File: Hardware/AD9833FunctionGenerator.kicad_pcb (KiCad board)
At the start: 2 copper layers, 125.7 x 114.3 mm, 53 parts, among them U1 LM7805_TO220

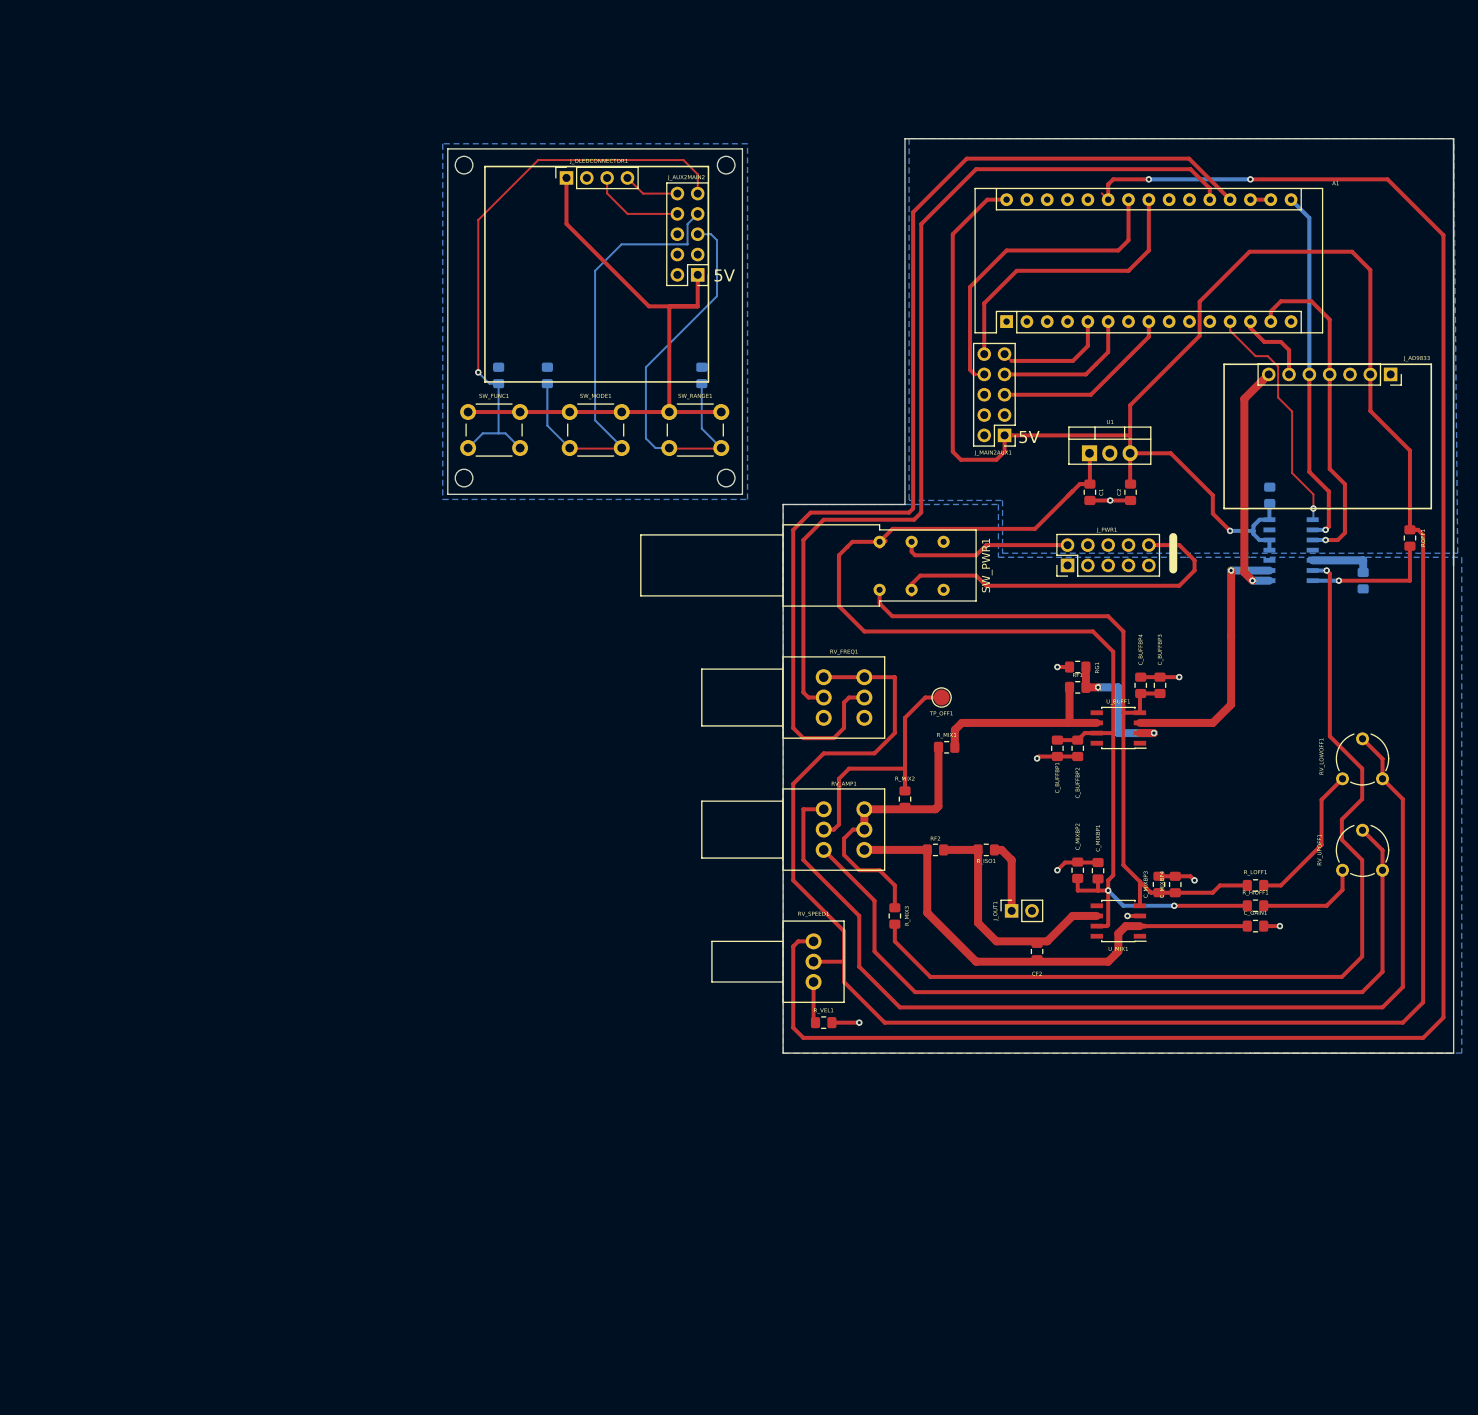
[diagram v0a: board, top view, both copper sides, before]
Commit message: Updated potentimeter footprints
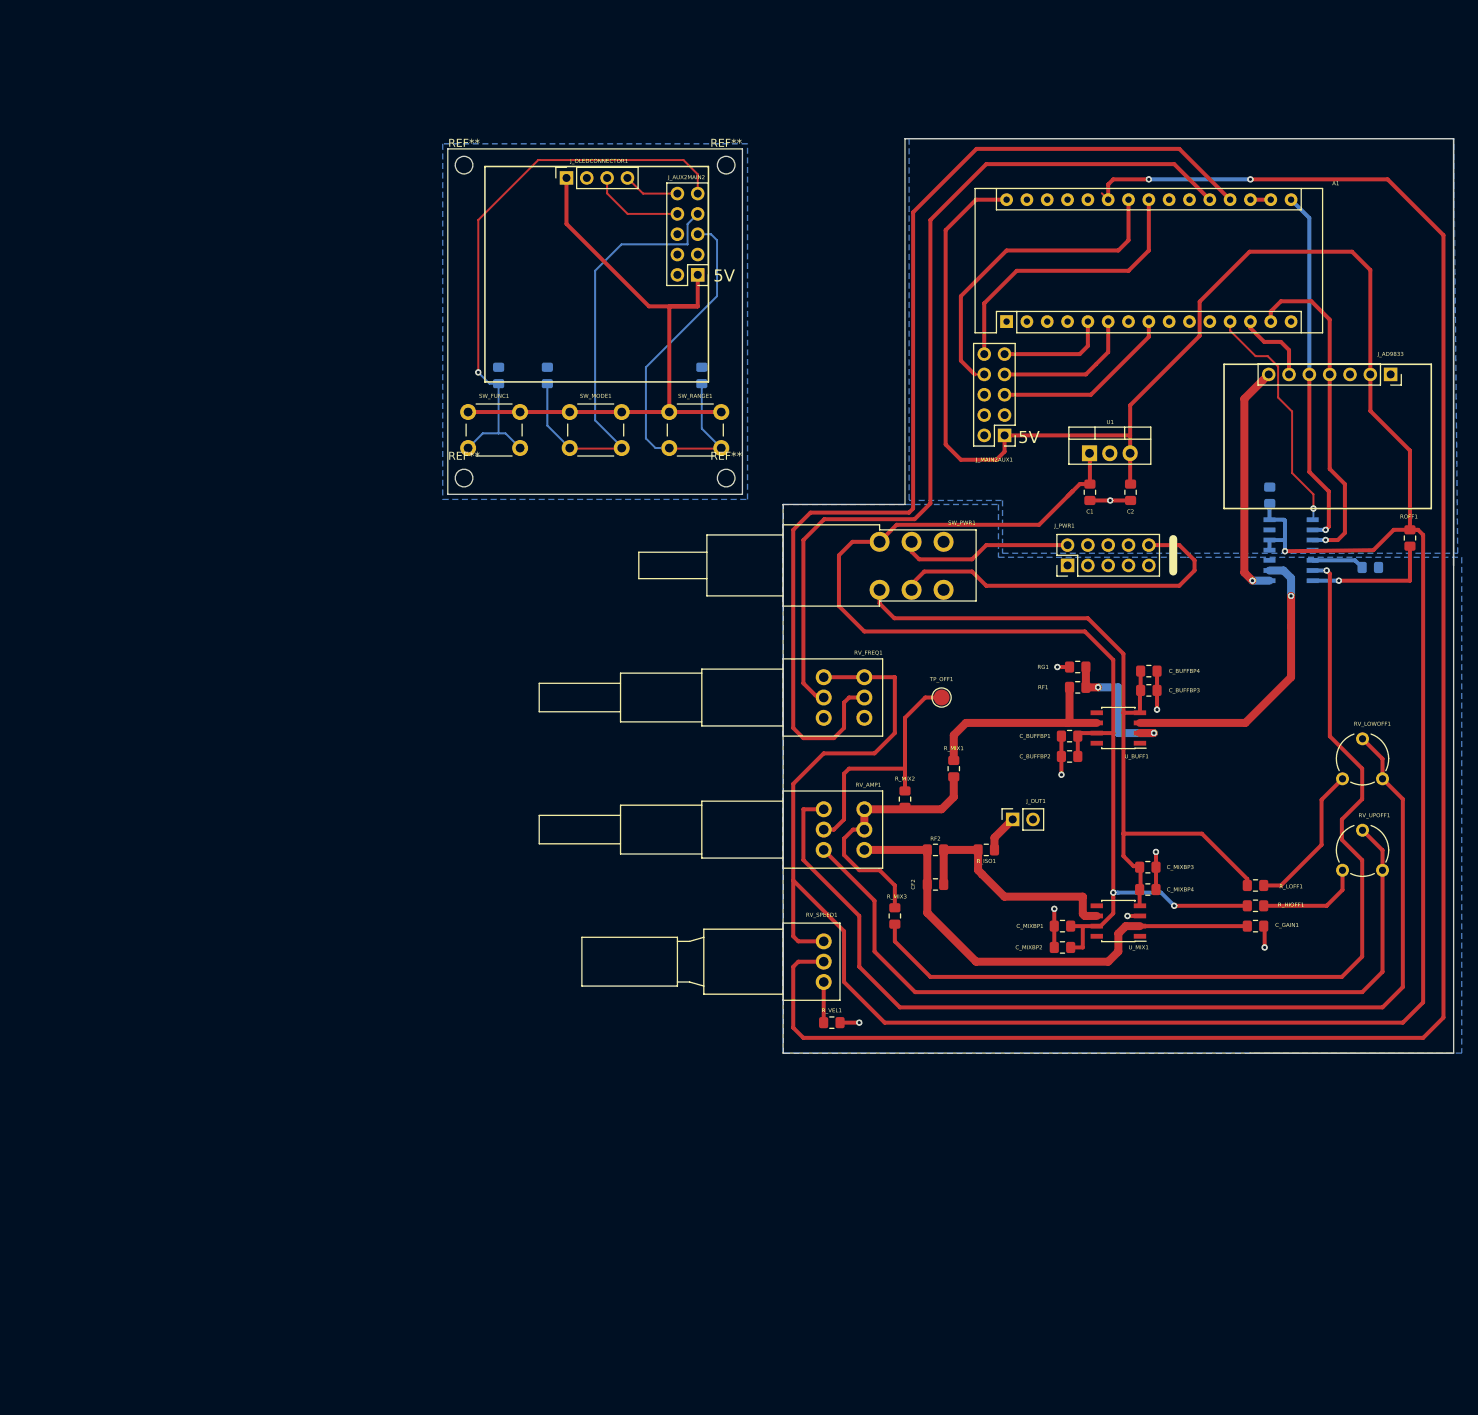
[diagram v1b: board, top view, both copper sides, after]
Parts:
- moved CF2 15.2 mm to (138.4, 128.8), turned to 180 degrees
- moved J_OUT1 11.4 mm to (148.1, 120.7)
- moved C_MIXBP2 9.84 mm to (154.3, 136.7), turned to 180 degrees
- moved C_MIXBP1 8.23 mm to (154.3, 134.0), turned to 180 degrees
- moved C_MIXBP4 3.49 mm to (165.0, 129.4), turned to 0 degrees
- moved R_MIX1 2.81 mm to (140.7, 114.3), turned to 270 degrees
- moved C_MIXBP3 2.57 mm to (165.0, 126.6), turned to 0 degrees
- moved C_BUFFBP1 2.16 mm to (155.2, 110.2), turned to 180 degrees
- moved C_BUFFBP4 2.05 mm to (165.1, 102.1), turned to 0 degrees
- moved ROFF2 1.88 mm to (192.8, 89.2), turned to 0 degrees
- moved C_BUFFBP3 1.53 mm to (165.1, 104.5), turned to 0 degrees
- moved C_BUFFBP2 1.44 mm to (155.2, 112.8), turned to 180 degrees
- moved R_VEL1 1.02 mm to (125.5, 146.1)
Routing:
- net /5V: track 375.8 -> 382.6 mm
- net /OutputSection/SIGOUT: track 9.03 -> 4.75 mm
- net /-12V: track 89.5 -> 92.5 mm
- net /DDS_REDUX: track 34.5 -> 37.2 mm
- net Net-(RV_AMP1-Pad5): track 35.1 -> 32.6 mm
- net /+12V: track 152.1 -> 150.6 mm
- net /FREQ2: track 115.4 -> 114.0 mm
- net Net-(ROFF2-Pad1): track 7.83 -> 6.55 mm
- net /VEL1: track 241.7 -> 240.4 mm
- net /AGND: track 28.5 -> 27.3 mm
- net /WAVEBTN: track 14.6 -> 13.4 mm
- net /FREQ1: track 135.8 -> 136.8 mm
- net /SCL: track 39.7 -> 40.6 mm
- net Net-(CF2-Pad1): track 30.5 -> 29.6 mm
- net Net-(RF1-Pad1): track 25.6 -> 26.2 mm

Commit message: Added third concentric dual pot for phase feature
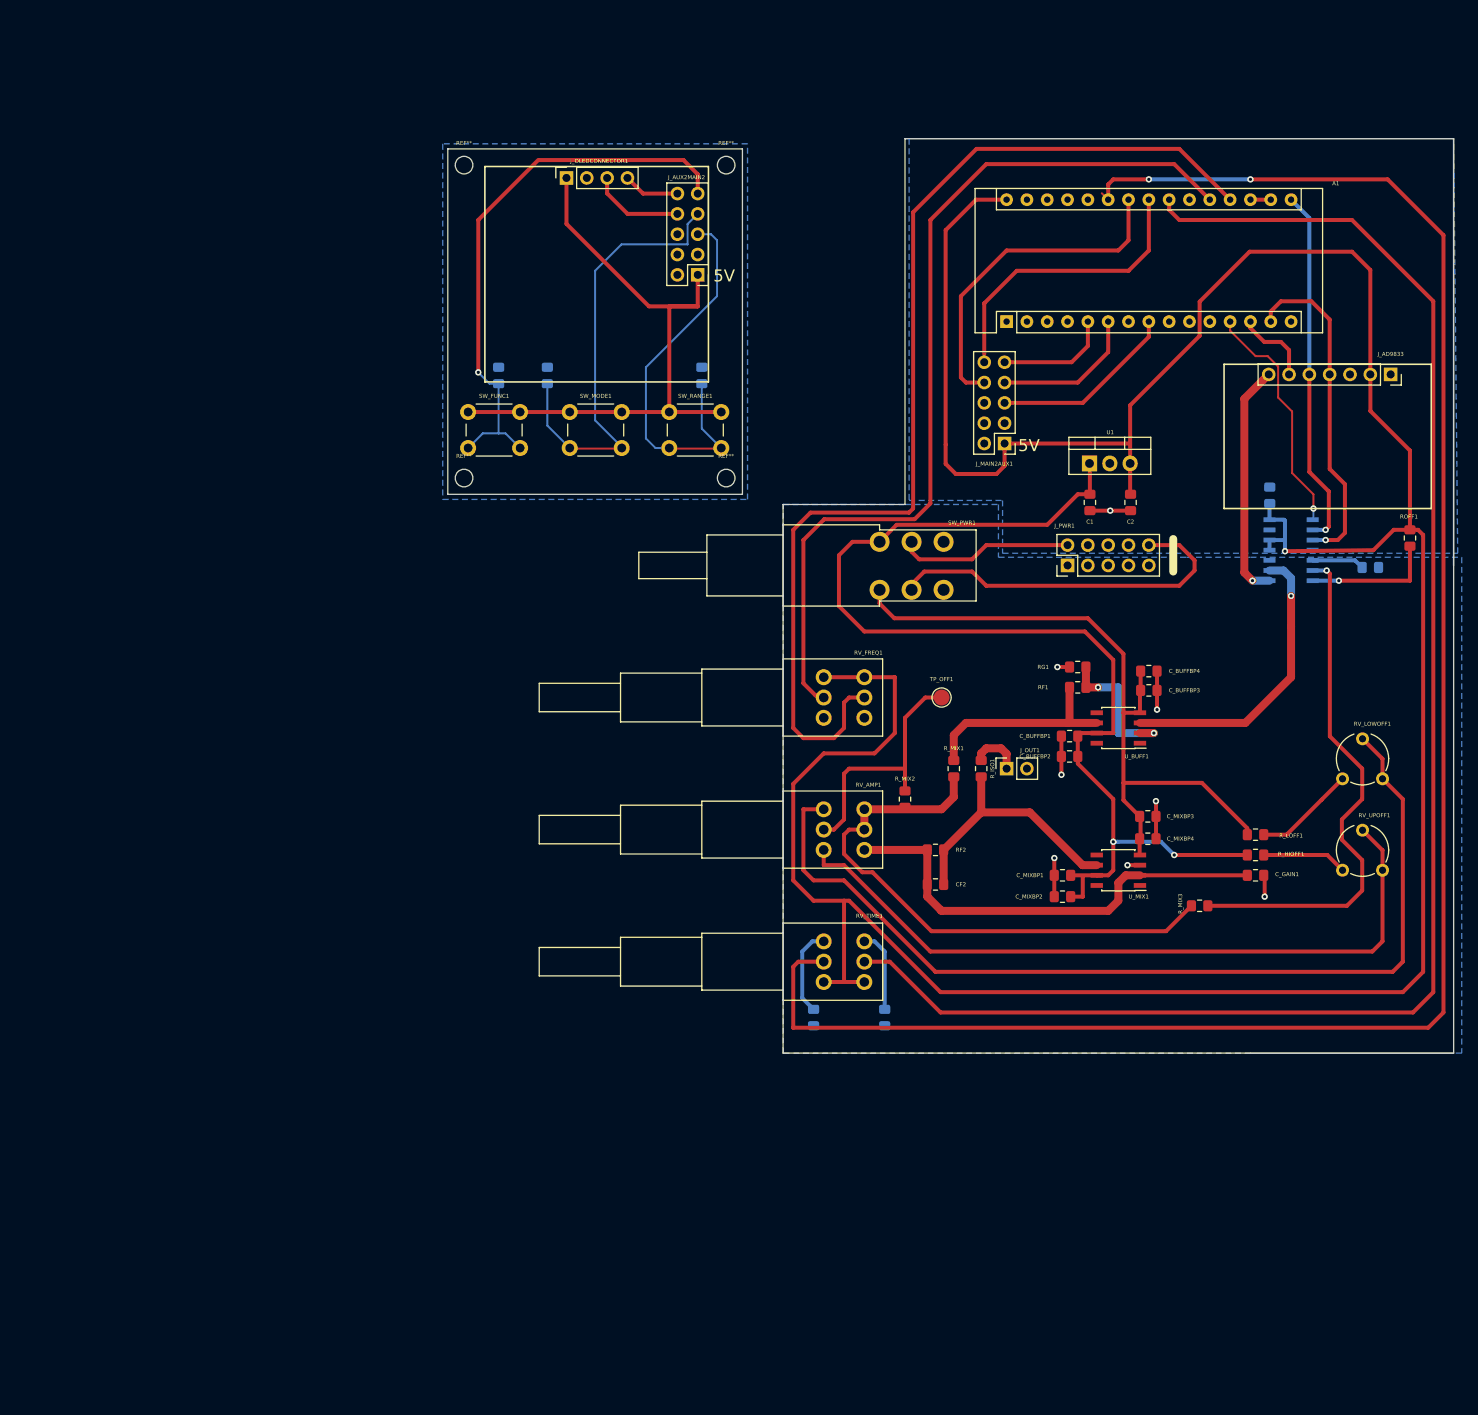
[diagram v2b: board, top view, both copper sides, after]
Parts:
- removed RV_SPEED1: R_POT, PTD901:PTD90
- added RV_TIME1: R_POT_Dual_Separate, PTH901:PTH901, F.Cu at (127.0, 138.4)
- added R_PHASE1: 100R, Resistor_SMD:R_0805_2012Metric_Pad1.15x1.40mm_HandSolder, B.Cu at (132.1, 145.4)
- R_VEL1: moved to B.Cu
- moved R_MIX3 38.1 mm to (171.4, 131.4), turned to 180 degrees
- moved R_ISO1 10.2 mm to (144.1, 114.3), turned to 270 degrees
- moved J_OUT1 6.40 mm to (147.3, 114.3)
- moved C_GAIN1 6.35 mm to (178.4, 127.6)
- moved C_MIXBP1 6.35 mm to (154.3, 127.6)
- moved C_MIXBP4 6.35 mm to (165.0, 123.1)
- moved C_MIXBP2 6.35 mm to (154.3, 130.3)
- moved C_MIXBP3 6.35 mm to (165.0, 120.3)
- moved R_HIOFF1 6.35 mm to (178.4, 125.1)
- moved R_LOFF1 6.35 mm to (178.4, 122.6)
- moved U_MIX1 6.35 mm to (161.3, 127.0)
- moved R_VEL1 2.37 mm to (123.2, 145.4), turned to 90 degrees
- moved C1 1.27 mm to (157.7, 81.0)
- moved C2 1.27 mm to (162.8, 81.0)
- moved U1 1.27 mm to (157.7, 76.1)
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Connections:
- net /FREQ1 renamed /FREQHI
- net /FREQ2 renamed /FREQLO
- A1 pad 22: (no net) -> /PHASE1
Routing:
- net /PHASE1: track 0.00 -> 200.2 mm
- net /OFFSETADJUST: track 117.4 -> 65.8 mm
- net Net-(RV_AMP1-Pad5): track 32.6 -> 70.8 mm
- net Net-(RV_TIME1-Pad6): track 0.00 -> 10.3 mm
- net Net-(RV_AMP1-Pad1): track 100.7 -> 91.7 mm
- net Net-(RV_AMP1-Pad3): track 129.3 -> 120.8 mm
- net /+12V: track 150.6 -> 142.8 mm
- net /-12V: track 92.5 -> 86.0 mm
- net Net-(RV_TIME1-Pad3): track 4.84 -> 11.0 mm
- net Net-(RV_LOWOFF1-Pad3): track 18.7 -> 12.7 mm
- net Net-(CF2-Pad2): track 61.7 -> 57.8 mm
- net Net-(CF2-Pad1): track 29.6 -> 32.6 mm
- net Net-(RV_UPOFF1-Pad3): track 13.1 -> 10.6 mm
- net /AGND: track 27.3 -> 24.9 mm, vias 8 -> 7
- net /OutputSection/SIGOUT: track 4.75 -> 6.45 mm
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
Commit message: Updated footprints
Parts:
- RV_LOWOFF1, RV_UPOFF1: footprint Potentiometer_THT:Potentiometer_Piher_PT-6-V_Vertical -> Potentiometer_THT:Potentiometer_Piher_PT-6-H_Horizontal
- moved RV_LOWOFF1 7.41 mm to (190.5, 109.2), turned to 0 degrees
- moved RV_UPOFF1 4.58 mm to (190.5, 124.5), turned to 0 degrees
- moved SW_PWR1 1.27 mm to (130.2, 88.9)
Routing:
- net /OFFSETADJUST: track 65.8 -> 71.5 mm
- net Net-(RV_AMP1-Pad3): track 120.8 -> 124.2 mm
- net Net-(RV_UPOFF1-Pad3): track 10.6 -> 12.8 mm
- net /VEL1: track 239.0 -> 241.0 mm
- net Net-(RV_LOWOFF1-Pad3): track 12.7 -> 14.5 mm
- net Net-(RV_AMP1-Pad1): track 91.7 -> 90.4 mm
